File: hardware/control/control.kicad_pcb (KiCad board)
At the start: 2 copper layers, 110 x 70 mm, 59 parts, among them J1 Conn_01x05_Male, J2 CANPWR, J3 CANGND, J4 RJ45, J5 RJ45, J6 Conn_02x03_Odd_Even, J7 DCDC-PWM, J8 DCDC-MEASURES, J9 display, Q1 BSS123, SW1 next, SW2 select, U1 2.048V, U2 AP63200WU, U3 PIC18F27Q84, U4 TLE9250VSJXUMA1, Y1 10Mhz

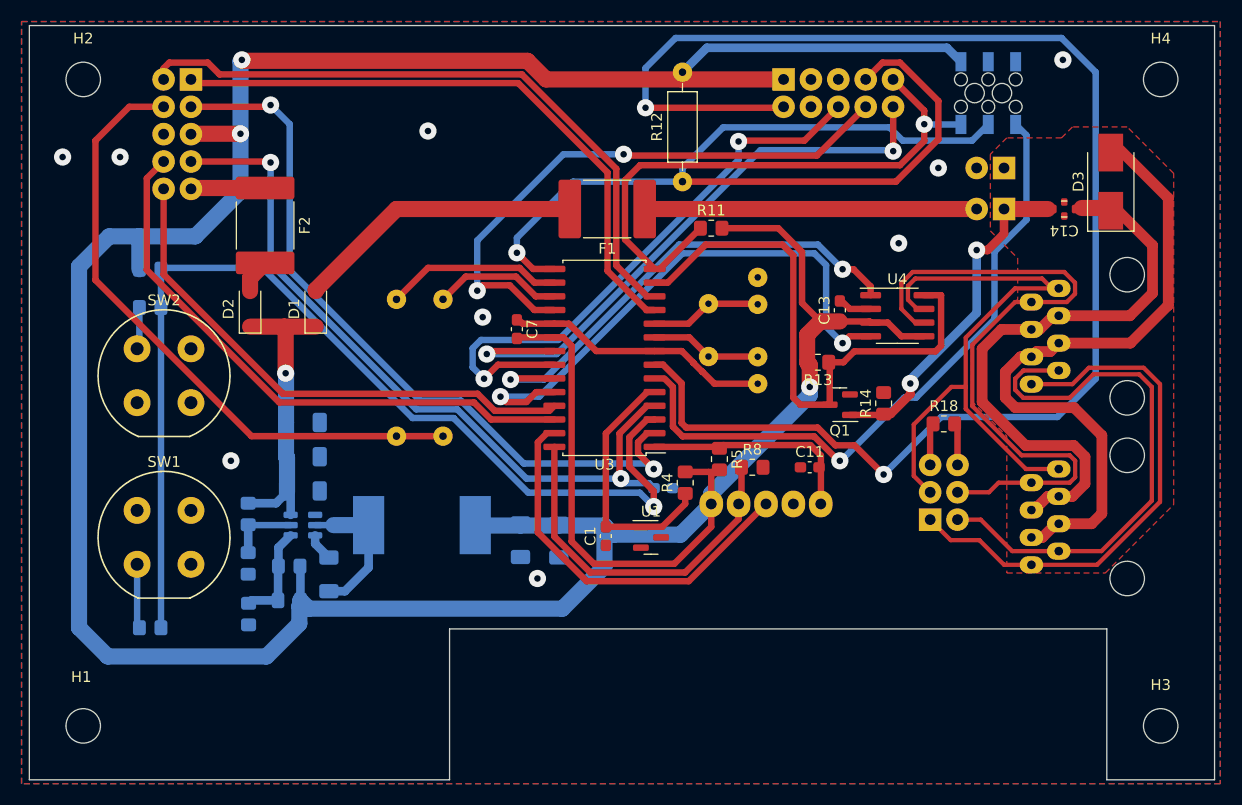
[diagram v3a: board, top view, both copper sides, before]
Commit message: Re-annotate schematics
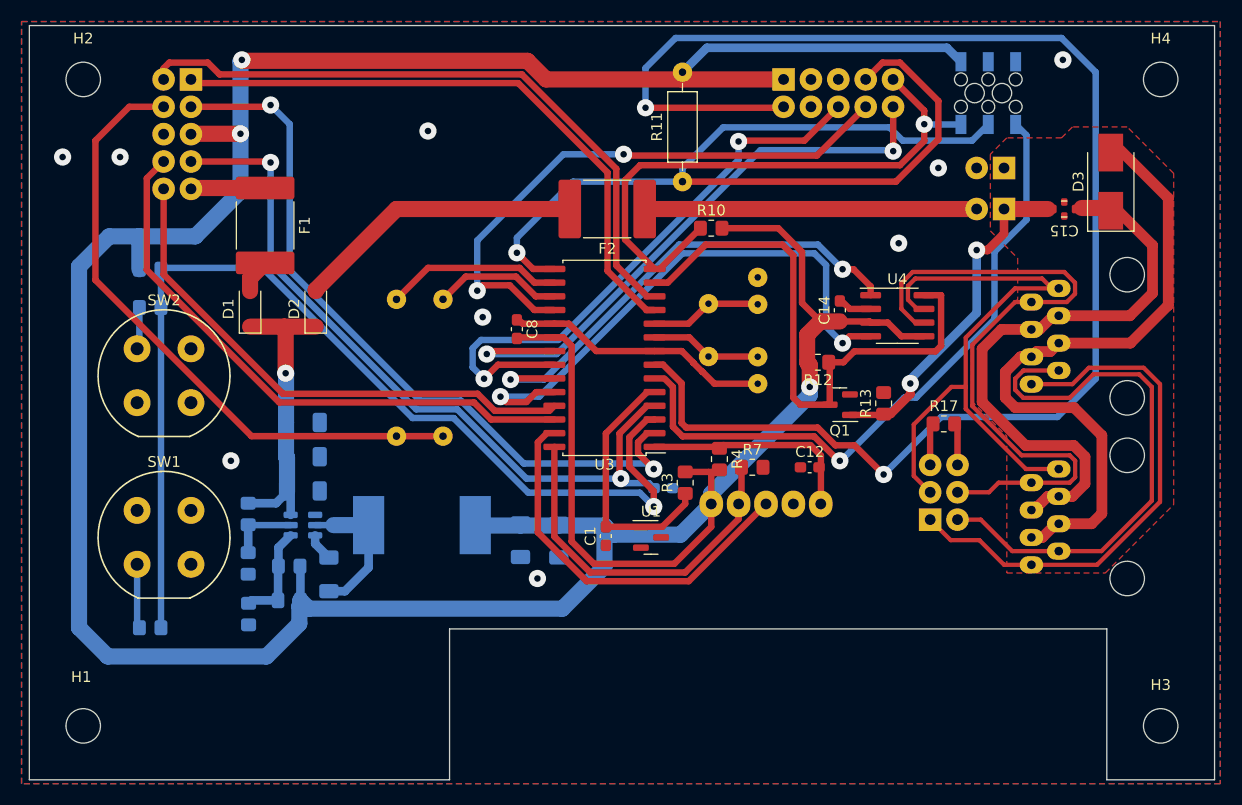
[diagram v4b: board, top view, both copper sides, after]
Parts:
- renumbered C9 to C10, C10 to C11, C11 to C12, C12 to C13, C13 to C14, C14 to C15, C15 to C5, C5 to C6, C6 to C7, C7 to C8, C8 to C9, D2 to D1, D1 to D2, F2 to F1, F1 to F2, J7 to J2, J9 to J3, J8 to J4, J2 to J5, J3 to J6, J4 to J7, J5 to J8, J6 to J9, R2 to R1, R11 to R10, R12 to R11, R13 to R12, R14 to R13, R15 to R14, R16 to R15, R17 to R16, R18 to R17, R3 to R2, R4 to R3, R5 to R4, R6 to R5, R7 to R6, R8 to R7, R9 to R8, R10 to R9

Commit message: Connect mounting holes to GND
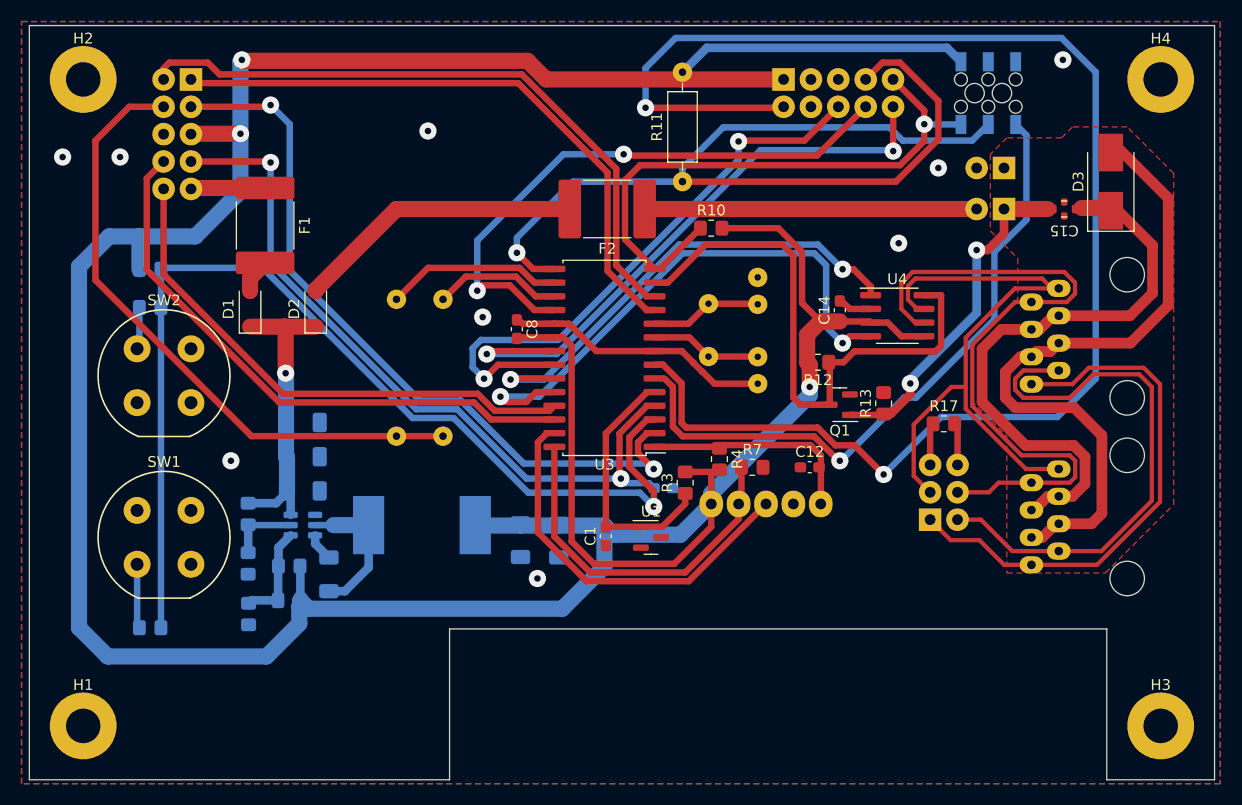
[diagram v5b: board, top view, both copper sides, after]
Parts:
- H1, H2, H3, H4: value MountingHole -> MountingHole_Pad; footprint MountingHole:MountingHole_3.2mm_M3_DIN965 -> MountingHole:MountingHole_3.2mm_M3_DIN965_Pad
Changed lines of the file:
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@@
     )
   )
-  (footprint "MountingHole:MountingHole_3.2mm_M3_DIN965" locked (layer "F.Cu")
+  (footprint "MountingHole:MountingHole_3.2mm_M3_DIN965_Pad" locked (layer "F.Cu")
     (at 155 145)
-    (descr "Mounting Hole 3.2mm, no annular, M3, DIN965")
-    (tags "mounting hole 3.2mm no annular m3 din965")
+    (descr "Mounting Hole 3.2mm, M3, DIN965")
+    (tags "mounting hole 3.2mm m3 din965")
     (property "Sheetfile" "control.kicad_sch")
     (property "Sheetname" "")
@@
       (effects (font (size 1 1) (thickness 0.15)))
     )
-    (fp_text value "MountingHole" (at 0 3.8) (layer "F.Fab")
+    (fp_text value "MountingHole_Pad" (at 0 3.8) (layer "F.Fab")
       (effects (font (size 1 1) (thickness 0.15)))
     )
@@
     (fp_circle (center 0 0) (end 2.8 0) (layer "Cmts.User") (width 0.15) (fill none))
     (fp_circle (center 0 0) (end 3.05 0) (layer "F.CrtYd") (width 0.05) (fill none))
-    (pad "" np_thru_hole circle locked (at 0 0) (size 3.2 3.2) (drill 3.2) (layers *.Cu *.Mask))
+    (pad "1" thru_hole circle locked (at 0 0) (size 6.2 6.2) (drill 3.2) (layers *.Cu *.Mask)
+      (net 2 "GND") (pinfunction "1") (pintype "input"))
   )
   (footprint "Resistor_SMD:R_0805_2012Metric_Pad1.20x1.40mm_HandSolder" (layer "F.Cu")
@@
     )
   )
-  (footprint "MountingHole:MountingHole_3.2mm_M3_DIN965" locked (layer "F.Cu")
+  (footprint "MountingHole:MountingHole_3.2mm_M3_DIN965_Pad" locked (layer "F.Cu")
     (at 55 85)
-    (descr "Mounting Hole 3.2mm, no annular, M3, DIN965")
-    (tags "mounting hole 3.2mm no annular m3 din965")
+    (descr "Mounting Hole 3.2mm, M3, DIN965")
+    (tags "mounting hole 3.2mm m3 din965")
     (property "Sheetfile" "control.kicad_sch")
     (property "Sheetname" "")
@@
       (effects (font (size 1 1) (thickness 0.15)))
     )
-    (fp_text value "MountingHole" (at 0 3.8) (layer "F.Fab")
+    (fp_text value "MountingHole_Pad" (at 0 3.8) (layer "F.Fab")
       (effects (font (size 1 1) (thickness 0.15)))
     )
@@
     (fp_circle (center 0 0) (end 2.8 0) (layer "Cmts.User") (width 0.15) (fill none))
     (fp_circle (center 0 0) (end 3.05 0) (layer "F.CrtYd") (width 0.05) (fill none))
-    (pad "" np_thru_hole circle locked (at 0 0) (size 3.2 3.2) (drill 3.2) (layers *.Cu *.Mask))
-  )
-  (footprint "MountingHole:MountingHole_3.2mm_M3_DIN965" locked (layer "F.Cu")
+    (pad "1" thru_hole circle locked (at 0 0) (size 6.2 6.2) (drill 3.2) (layers *.Cu *.Mask)
+      (net 2 "GND") (pinfunction "1") (pintype "input"))
+  )
+  (footprint "MountingHole:MountingHole_3.2mm_M3_DIN965_Pad" locked (layer "F.Cu")
     (at 55 145)
-    (descr "Mounting Hole 3.2mm, no annular, M3, DIN965")
-    (tags "mounting hole 3.2mm no annular m3 din965")
+    (descr "Mounting Hole 3.2mm, M3, DIN965")
+    (tags "mounting hole 3.2mm m3 din965")
     (property "Sheetfile" "control.kicad_sch")
     (property "Sheetname" "")
     (attr exclude_from_pos_files)
-    (fp_text reference "H1" (at -0.188 -4.538) (layer "F.SilkS")
-      (effects (font (size 1 1) (thickness 0.15)))
-    )
-    (fp_text value "MountingHole" (at 0 3.8) (layer "F.Fab")
+    (fp_text reference "H1" (at 0 -3.8) (layer "F.SilkS")
+      (effects (font (size 1 1) (thickness 0.15)))
+    )
+    (fp_text value "MountingHole_Pad" (at 0 3.8) (layer "F.Fab")
       (effects (font (size 1 1) (thickness 0.15)))
     )
@@
     (fp_circle (center 0 0) (end 2.8 0) (layer "Cmts.User") (width 0.15) (fill none))
     (fp_circle (center 0 0) (end 3.05 0) (layer "F.CrtYd") (width 0.05) (fill none))
-    (pad "" np_thru_hole circle locked (at 0 0) (size 3.2 3.2) (drill 3.2) (layers *.Cu *.Mask))
+    (pad "1" thru_hole circle locked (at 0 0) (size 6.2 6.2) (drill 3.2) (layers *.Cu *.Mask)
+      (net 2 "GND") (pinfunction "1") (pintype "input"))
   )
   (footprint "Package_SO:SOIC-8_3.9x4.9mm_P1.27mm" (layer "F.Cu")
@@
     )
   )
-  (footprint "MountingHole:MountingHole_3.2mm_M3_DIN965" locked (layer "F.Cu")
+  (footprint "MountingHole:MountingHole_3.2mm_M3_DIN965_Pad" locked (layer "F.Cu")
     (at 155 85)
-    (descr "Mounting Hole 3.2mm, no annular, M3, DIN965")
-    (tags "mounting hole 3.2mm no annular m3 din965")
+    (descr "Mounting Hole 3.2mm, M3, DIN965")
+    (tags "mounting hole 3.2mm m3 din965")
     (property "Sheetfile" "control.kicad_sch")
     (property "Sheetname" "")
@@
       (effects (font (size 1 1) (thickness 0.15)))
     )
-    (fp_text value "MountingHole" (at 0 3.8) (layer "F.Fab")
+    (fp_text value "MountingHole_Pad" (at 0 3.8) (layer "F.Fab")
       (effects (font (size 1 1) (thickness 0.15)))
     )
@@
     (fp_circle (center 0 0) (end 2.8 0) (layer "Cmts.User") (width 0.15) (fill none))
     (fp_circle (center 0 0) (end 3.05 0) (layer "F.CrtYd") (width 0.05) (fill none))
-    (pad "" np_thru_hole circle locked (at 0 0) (size 3.2 3.2) (drill 3.2) (layers *.Cu *.Mask))
+    (pad "1" thru_hole circle locked (at 0 0) (size 6.2 6.2) (drill 3.2) (layers *.Cu *.Mask)
+      (net 2 "GND") (pinfunction "1") (pintype "input"))
   )
   (footprint "Capacitor_SMD:C_0603_1608Metric_Pad1.08x0.95mm_HandSolder" (layer "F.Cu")

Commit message: Change some resistor values to match available ones.
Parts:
- R5: value 157k -> 158k
- R9: value 8.1K -> 8.2K
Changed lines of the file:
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@@
       (effects (font (size 1 1) (thickness 0.15)) (justify mirror))
     )
-    (fp_text value "8.1K" (at 6.35 -2.72 90) (layer "B.Fab")
+    (fp_text value "8.2K" (at 6.35 -2.72 90) (layer "B.Fab")
       (effects (font (size 1 1) (thickness 0.15)) (justify mirror))
     )
@@
       (effects (font (size 1 1) (thickness 0.15)) (justify mirror))
     )
-    (fp_text value "157k" (at 0 -1.65) (layer "B.Fab")
-      (effects (font (size 1 1) (thickness 0.15)) (justify mirror))
-    )
+    (fp_text value "158k" (at 0 -1.65) (layer "B.Fab")
+      (effects (font (size 1 1) (thickness 0.15)) (justify mirror))
+    )

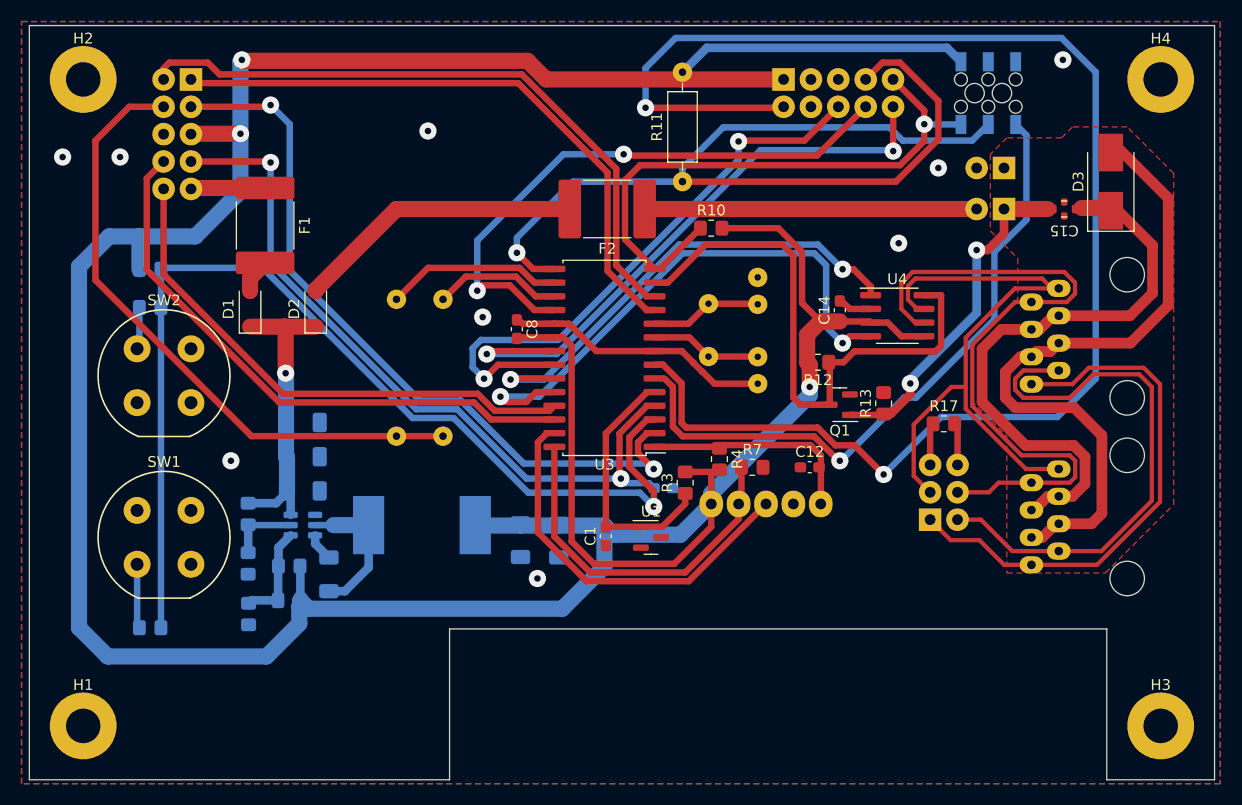
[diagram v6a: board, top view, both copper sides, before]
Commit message: control: rework tracks, increase clearance where possible.
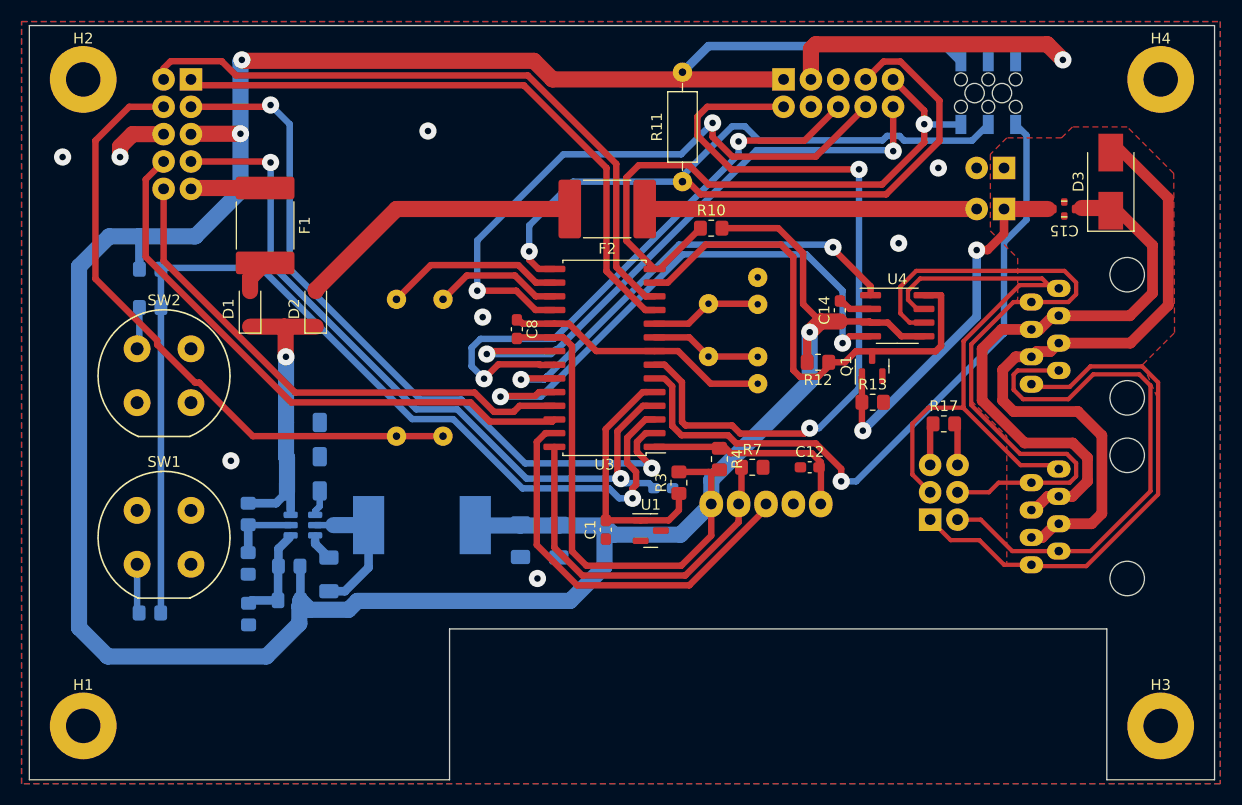
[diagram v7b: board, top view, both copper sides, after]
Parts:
- moved Q1 4.67 mm to (128.2, 111.6), turned to 90 degrees
- moved R15 1.37 mm to (61.2, 134.5)
- moved R13 1.02 mm to (128.3, 115.0), turned to 0 degrees
- moved U1 0.64 mm to (107.7, 126.9)
- moved C1 0.58 mm to (103.5, 126.8)
- moved R3 0.58 mm to (110.3, 122.4)
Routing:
- net TH: track 140.1 -> 72.3 mm
- net GND: track 28.1 -> 63.0 mm
- net /!CANOK: track 52.8 -> 46.6 mm
- net BTN_IN: track 98.5 -> 93.7 mm
- net +5V: track 328.2 -> 332.8 mm
- net /+12CAN: track 31.8 -> 35.8 mm
- net ~{RST_DISP}: track 61.1 -> 64.6 mm
- net /~{PAC_DOWN}: track 54.3 -> 57.1 mm
- net /CANH: track 57.8 -> 56.2 mm
- net SCL: track 54.3 -> 55.9 mm
- net /CANTX: track 45.1 -> 43.7 mm
- net Net-(R15-Pad2): track 5.68 -> 4.33 mm
- net /PWM_OFF: track 60.4 -> 61.5 mm
- net /PGC: track 35.6 -> 36.6 mm
- net /PGD: track 33.4 -> 34.4 mm
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
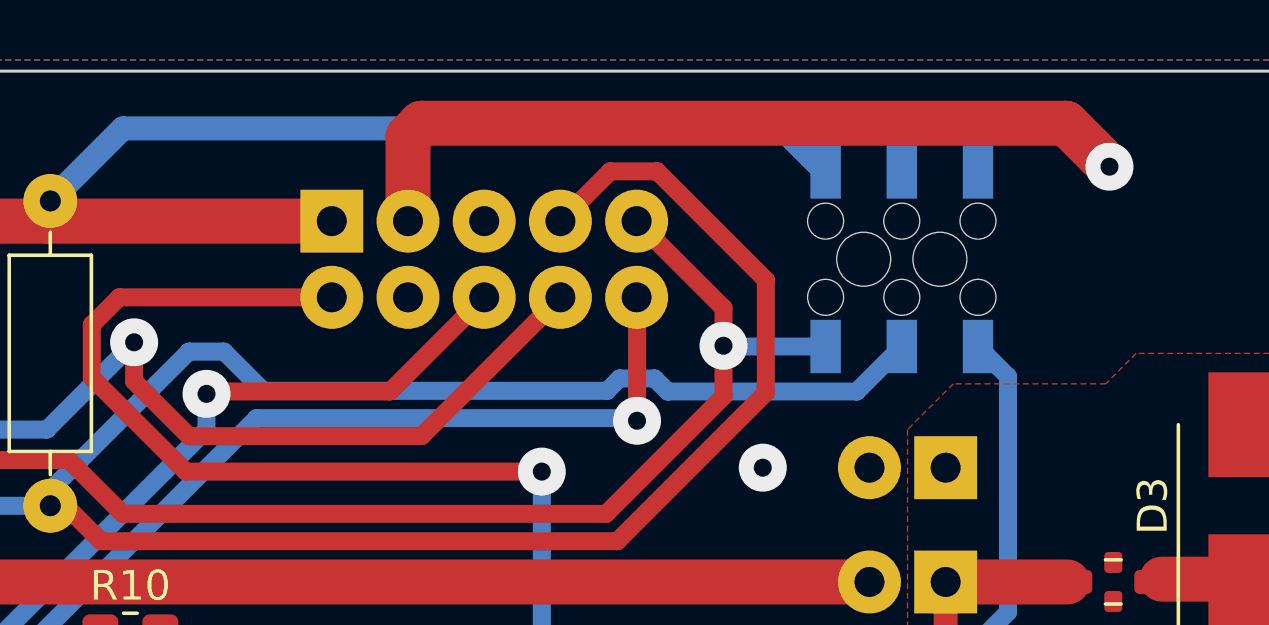
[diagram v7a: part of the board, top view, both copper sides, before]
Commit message: *: connect unused connectors pins to GND
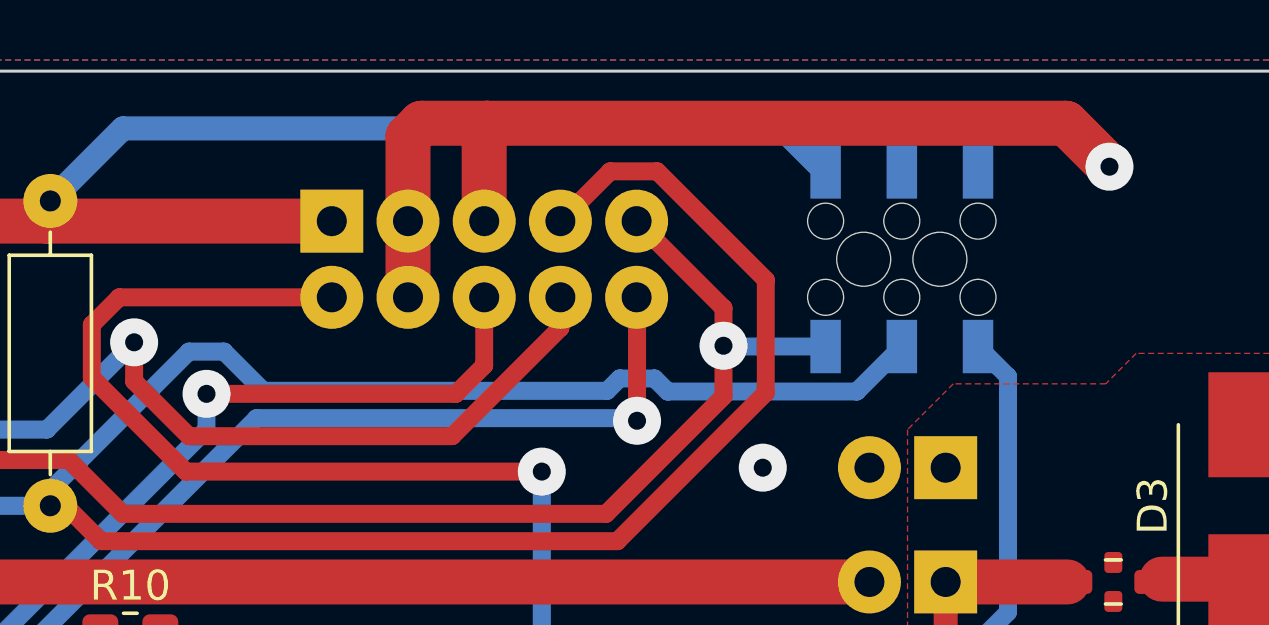
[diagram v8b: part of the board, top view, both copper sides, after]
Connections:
- J3 pad 2: unconnected-(J3-Pad2) -> GND
- J4 pad 4: unconnected-(J4-Pad4) -> GND
- J4 pad 5: unconnected-(J4-Pad5) -> GND
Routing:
- net GND: track 63.0 -> 68.8 mm
- net AL2: track 54.5 -> 55.8 mm
- net /~{PAC_DOWN}: track 57.1 -> 57.7 mm
